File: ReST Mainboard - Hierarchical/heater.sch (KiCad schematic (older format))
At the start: 40 parts, among them P27 CONN_02X06, P29 CONN_01X02, P30 CONN_01X02, P31 CONN_01X02, Q10 Q_AOT240L, Q11 Q_AOT240L, Q12 Q_AOT240L, Q7 Q_BSH105/IRLML2502, Q8 Q_BSH105/IRLML2502, Q9 Q_BSH105/IRLML2502

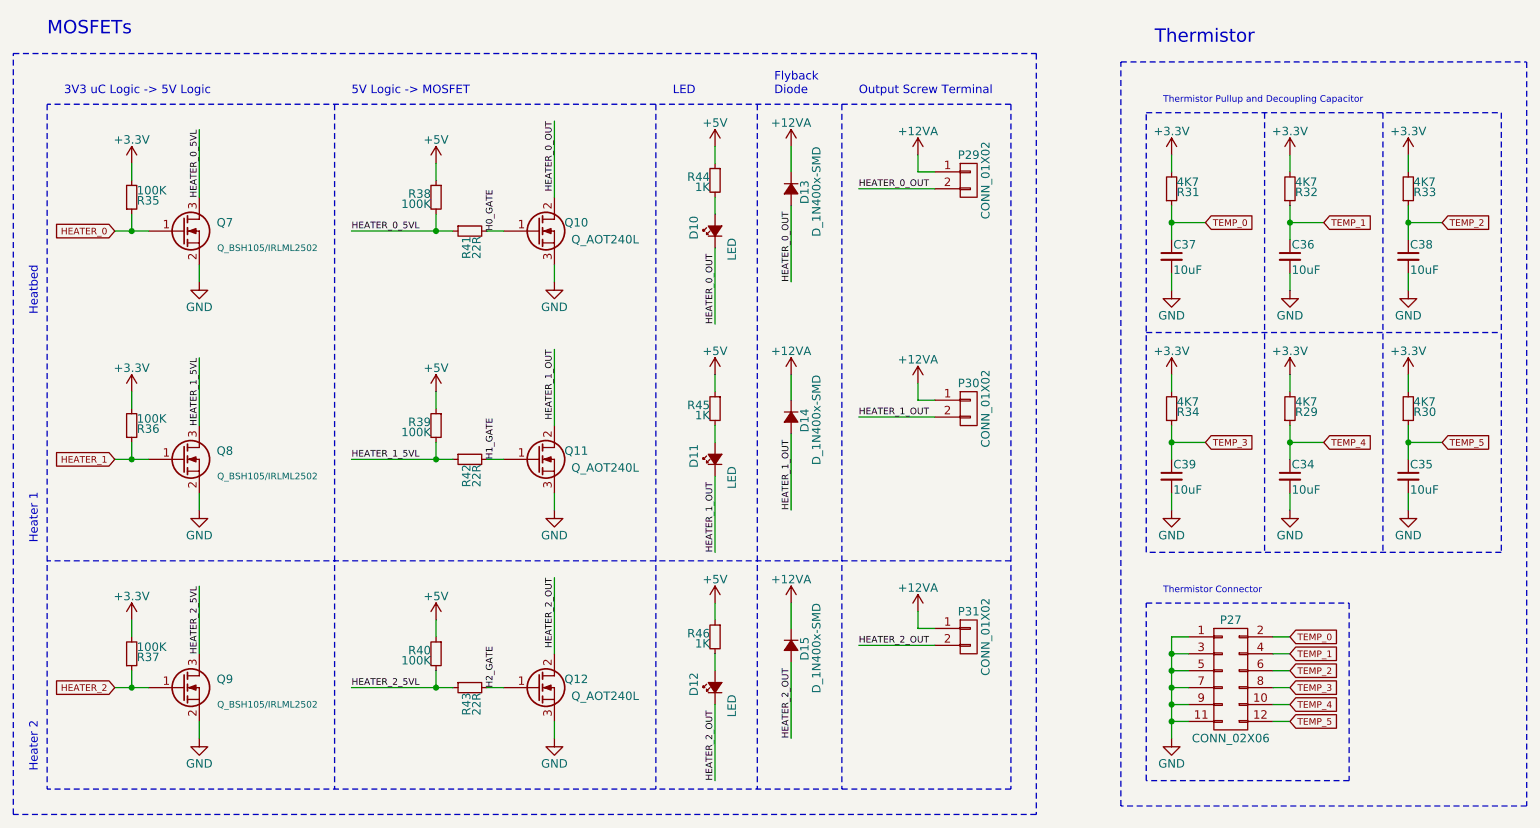
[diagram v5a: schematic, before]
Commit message: changes in footprints of heater part and misc. stuff
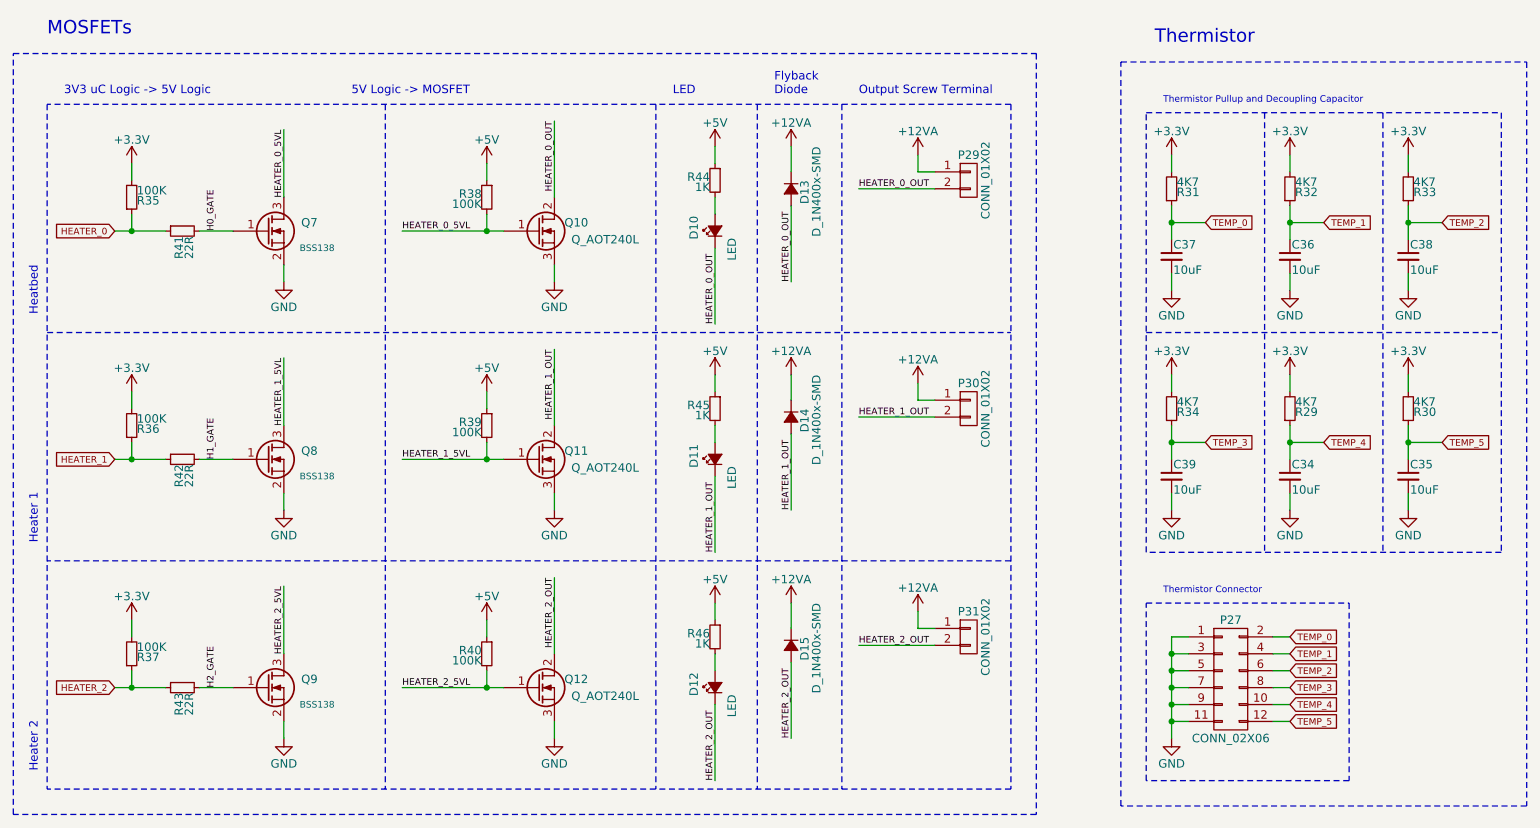
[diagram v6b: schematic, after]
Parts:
- Q7, Q8, Q9: value Q_BSH105/IRLML2502 -> BSS138
- R35, R36, R37, R38, R39, R40, R41, R42, R43, R44, R45, R46: footprint Resistors_SMD:R_0603_HandSoldering -> Resistors_SMD:R_0805_HandSoldering
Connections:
- net H0_GATE: now also Q7.1 (G); no longer Q10.1 (G)
- net H1_GATE: now also Q8.1 (G); no longer Q11.1 (G)
- net H2_GATE: now also Q9.1 (G); no longer Q12.1 (G)
- net HEATER_0: now also R41.1; no longer Q7.1 (G)
- net HEATER_0_5VL: now also Q10.1 (G); no longer R41.1
- net HEATER_1: now also R42.1; no longer Q8.1 (G)
- net HEATER_1_5VL: now also Q11.1 (G); no longer R42.1
- net HEATER_2: now also R43.1; no longer Q9.1 (G)
- net HEATER_2_5VL: now also Q12.1 (G); no longer R43.1
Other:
- moved on the sheet: Q7, Q8, Q9, R38, R39, R40, R41, R42, R43
